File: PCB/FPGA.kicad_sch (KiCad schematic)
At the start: 7 parts

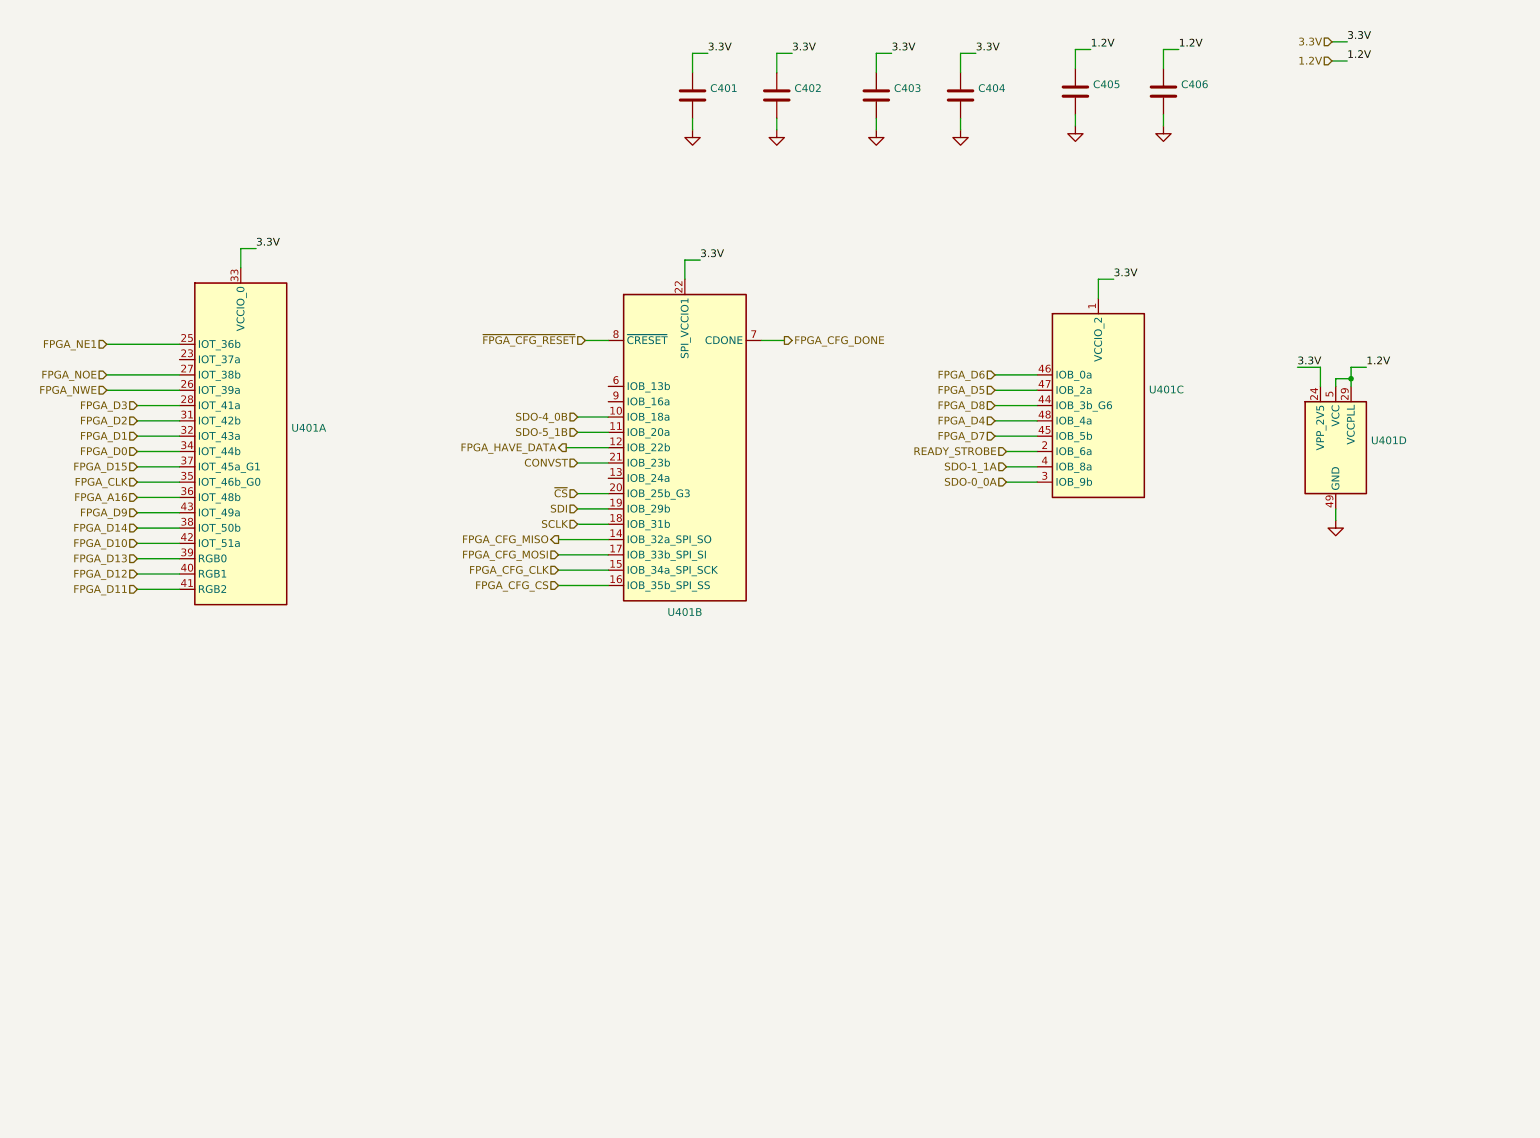
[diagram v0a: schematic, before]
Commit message: New version with FTDI chip instead of STM32 and ICE40HX FPGA instead of slower ones
Signed-off-by: Alexis Jeandet <alexis.jeandet@member.fsf.org>
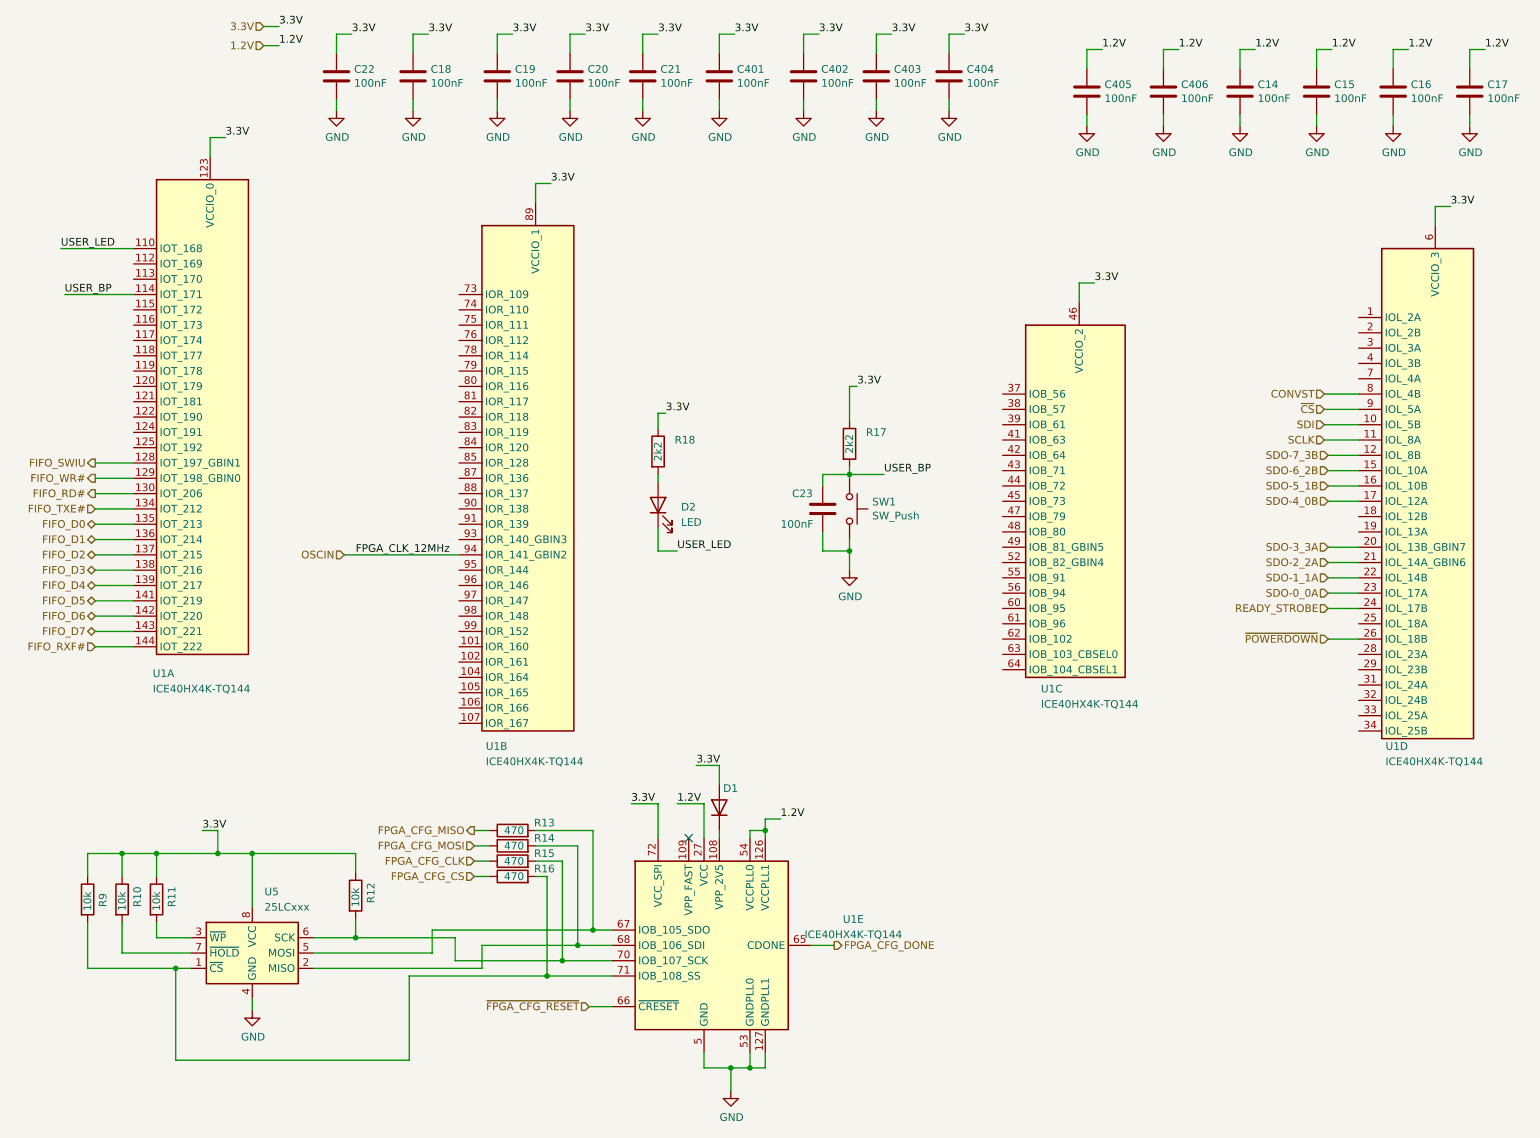
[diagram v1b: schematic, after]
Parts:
- removed U401: (no value), symbol FPGA_Lattice:ICE40UP5K-SG48ITR
- added C14, C15, C16, C17, C18, C19, C20, C21, C22, C23: 100nF, Capacitor_SMD:C_0402_1005Metric_Pad0.74x0.62mm_HandSolder, symbol Device:C
- added D1: 1N4148WT, Diode_SMD:D_SOD-523, symbol Diode:1N4148WT
- added D2: LED, Diode_SMD:D_0603_1608Metric_Pad1.05x0.95mm_HandSolder, symbol Device:LED
- added R10, R11, R12, R9: 10k, Resistor_SMD:R_0402_1005Metric_Pad0.72x0.64mm_HandSolder, symbol Device:R
- added R13, R14, R15, R16: 470, Resistor_SMD:R_0402_1005Metric_Pad0.72x0.64mm_HandSolder, symbol Device:R
- added R17, R18: 2k2, Resistor_SMD:R_0402_1005Metric_Pad0.72x0.64mm_HandSolder, symbol Device:R
- added SW1: SW_Push, Button_Switch_SMD:SW_SPST_TL3342, symbol Switch:SW_Push
- added U1: ICE40HX4K-TQ144, Package_QFP:TQFP-144_20x20mm_P0.5mm, symbol FPGA_Lattice:ICE40HX4K-TQ144
- added U5: 25LCxxx, Package_SO:SOP-8_3.9x4.9mm_P1.27mm, symbol Memory_EEPROM:25LCxxx
- C401, C402, C403, C404, C405, C406: value (none) -> 100nF; footprint (none) -> Capacitor_SMD:C_0402_1005Metric_Pad0.74x0.62mm_HandSolder
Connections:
- net 1.2V: now also C14.1, C15.1, C16.1, C17.1, U1.111 (VCC), U1.126 (VCCPLL1), U1.27 (VCC), U1.40 (VCC), U1.54 (VCCPLL0), U1.92 (VCC)
- net 3.3V: now also C18.1, C19.1, C20.1, C21.1, C22.1, D1.2 (A), R10.1, R11.1, R12.1, R17.1, R18.1, R9.1, U1.100 (VCCIO_1), U1.123 (VCCIO_0), U1.131 (VCCIO_0), U1.30 (VCCIO_3), U1.46 (VCCIO_2), U1.57 (VCCIO_2), U1.6 (VCCIO_3), U1.72 (VCC_SPI), U1.89 (VCCIO_1), U5.8 (VCC)
- net CONVST: now also U1.8 (IOL_4B)
- net FPGA_CFG_CLK: now also R15.1
- net FPGA_CFG_CS: now also R16.1
- net FPGA_CFG_DONE: now also U1.65 (CDONE)
- net FPGA_CFG_MISO: now also R13.1
- net FPGA_CFG_MOSI: now also R14.1
- net GND: now also C14.2, C15.2, C16.2, C17.2, C18.2, C19.2, C20.2, C21.2, C22.2, C23.2, SW1.2, U1.103 (GND), U1.127 (GNDPLL1), U1.13 (GND), U1.132 (GND), U1.14 (GND), U1.140 (GND), U1.5 (GND), U1.53 (GNDPLL0), U1.59 (GND), U1.69 (GND), U1.86 (GND), U5.4 (GND)
- net READY_STROBE: now also U1.24 (IOL_17B)
- net SCLK: now also U1.11 (IOL_8A)
- net SDI: now also U1.10 (IOL_5B)
- net SDO-0_0A: now also U1.23 (IOL_17A)
- net SDO-1_1A: now also U1.22 (IOL_14B)
- net SDO-4_0B: now also U1.17 (IOL_12A)
- net SDO-5_1B: now also U1.16 (IOL_10B)
- net ~{CS}: now also U1.9 (IOL_5A)
- net ~{FPGA_CFG_RESET}: now also U1.66 (~{CRESET})
- new net: D2.2 (A), R18.2
- new net: R11.2, U5.3 (~{WP})
- new net: D1.1 (K), U1.108 (VPP_2V5)
- new net: R13.2, U1.67 (IOB_105_SDO), U5.5 (MOSI)
- new net: R14.2, U1.68 (IOB_106_SDI), U5.2 (MISO)
- new net: R12.2, R15.2, U1.70 (IOB_107_SCK), U5.6 (SCK)
- new net: R16.2, R9.2, U1.71 (IOB_108_SS), U5.1 (~{CS})
- new net: R10.2, U5.7 (~{HOLD})
- new net FIFO_D0: U1.135 (IOT_213)
- new net FIFO_D1: U1.136 (IOT_214)
- new net FIFO_D2: U1.137 (IOT_215)
- new net FIFO_D3: U1.138 (IOT_216)
- new net FIFO_D4: U1.139 (IOT_217)
- new net FIFO_D5: U1.141 (IOT_219)
- new net FIFO_D6: U1.142 (IOT_220)
- new net FIFO_D7: U1.143 (IOT_221)
- new net FIFO_RD#: U1.130 (IOT_206)
- new net FIFO_RXF#: U1.144 (IOT_222)
- new net FIFO_SWIU: U1.128 (IOT_197_GBIN1)
- new net FIFO_TXE#: U1.134 (IOT_212)
- new net FIFO_WR#: U1.129 (IOT_198_GBIN0)
- new net OSCIN: U1.94 (IOR_141_GBIN2)
- new net SDO-2_2A: U1.21 (IOL_14A_GBIN6)
- new net SDO-3_3A: U1.20 (IOL_13B_GBIN7)
- new net SDO-6_2B: U1.15 (IOL_10A)
- new net SDO-7_3B: U1.12 (IOL_8B)
- new net USER_BP: C23.1, R17.2, SW1.1, U1.114 (IOT_171)
- new net USER_LED: D2.1 (K), U1.110 (IOT_168)
- new net ~{POWERDOWN}: U1.26 (IOL_18B)
- no-connect marks 0 -> 1
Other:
- moved on the sheet: C401, C402, C403, C404, C405

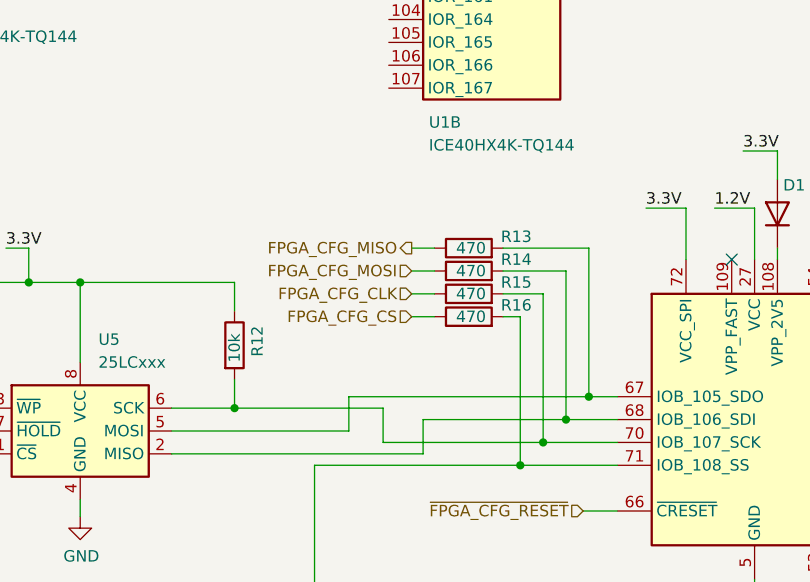
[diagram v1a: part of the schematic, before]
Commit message: adds UGA and few sch libs update
Signed-off-by: Alexis Jeandet <alexis.jeandet@member.fsf.org>
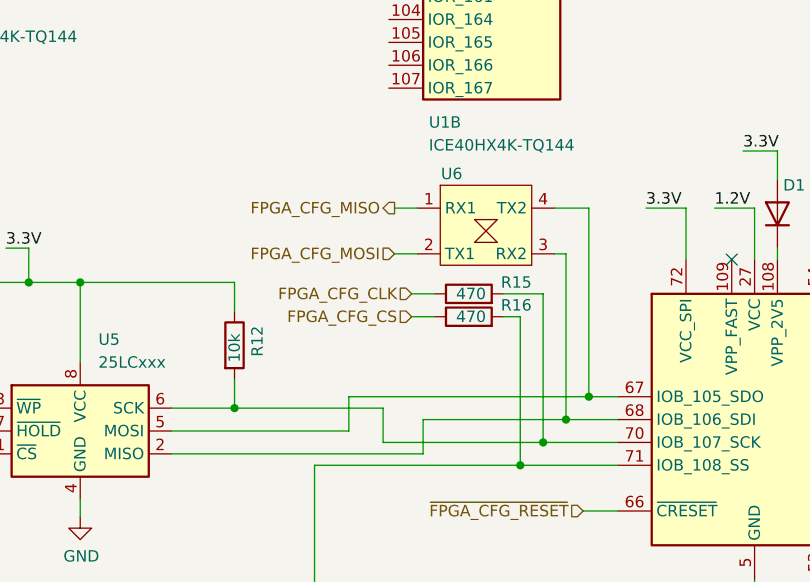
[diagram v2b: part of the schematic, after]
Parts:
- removed R13, R14: 470, Resistor_SMD:R_0402_1005Metric_Pad0.72x0.64mm_HandSolder, symbol Device:R
- added U6: UGA, UGA:UGA_0603, symbol UGA:UGA
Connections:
- net FPGA_CFG_MISO: now also U6.1 (RX1)
- net FPGA_CFG_MOSI: now also U6.2 (TX1)
- net at U1.67 (IOB_105_SDO), U5.5 (MOSI): now also U6.4 (TX2)
- net at U1.68 (IOB_106_SDI), U5.2 (MISO): now also U6.3 (RX2)
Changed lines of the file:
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@@
+    (stroke (width 0) (type default) (color 0 0 0 0))
+  )
+  (wire (pts (xy 114.935 149.225) (xy 113.665 149.225))
     (stroke (width 0) (type default) (color 0 0 0 0))
   )
@@
     (stroke (width 0) (type default) (color 0 0 0 0))
   )
+  (wire (pts (xy 114.935 149.225) (xy 114.935 167.64))
+    (stroke (width 0) (type default) (color 0 0 0 0))
+  )
   (wire (pts (xy 128.27 79.375) (xy 128.27 81.915))
     (stroke (width 0) (type default) (color 0 0 0 0))
@@
     (stroke (width 0) (type default) (color 0 0 0 0))
   )
-  (wire (pts (xy 107.95 148.59) (xy 117.475 148.59))
-    (stroke (width 0) (type default) (color 0 0 0 0))
-  )
-  (wire (pts (xy 97.79 151.13) (xy 100.33 151.13))
+  (wire (pts (xy 95.885 149.225) (xy 98.425 149.225))
     (stroke (width 0) (type default) (color 0 0 0 0))
   )
@@
     (stroke (width 0) (type default) (color 0 0 0 0))
   )
-  (wire (pts (xy 117.475 148.59) (xy 117.475 165.1))
-    (stroke (width 0) (type default) (color 0 0 0 0))
-  )
   (wire (pts (xy 90.805 165.1) (xy 117.475 165.1))
     (stroke (width 0) (type default) (color 0 0 0 0))
@@
     (stroke (width 0) (type default) (color 0 0 0 0))
   )
-  (wire (pts (xy 107.95 151.13) (xy 114.935 151.13))
-    (stroke (width 0) (type default) (color 0 0 0 0))
-  )
   (wire (pts (xy 60.96 152.4) (xy 78.105 152.4))
     (stroke (width 0) (type default) (color 0 0 0 0))
@@
     (stroke (width 0) (type default) (color 0 0 0 0))
   )
-  (wire (pts (xy 97.79 148.59) (xy 100.33 148.59))
+  (wire (pts (xy 95.885 144.145) (xy 98.425 144.145))
     (stroke (width 0) (type default) (color 0 0 0 0))
   )
@@
     (stroke (width 0) (type default) (color 0 0 0 0))
   )
+  (wire (pts (xy 113.665 144.145) (xy 117.475 144.145))
+    (stroke (width 0) (type default) (color 0 0 0 0))
+  )
   (wire (pts (xy 29.21 52.07) (xy 41.275 52.07))
     (stroke (width 0) (type default) (color 0 0 0 0))
@@
     (stroke (width 0) (type default) (color 0 0 0 0))
   )
-  (wire (pts (xy 114.935 151.13) (xy 114.935 167.64))
-    (stroke (width 0) (type default) (color 0 0 0 0))
-  )
   (wire (pts (xy 152.4 29.21) (xy 152.4 27.305))
     (stroke (width 0) (type default) (color 0 0 0 0))
@@
   )
   (wire (pts (xy 107.95 153.67) (xy 112.395 153.67))
+    (stroke (width 0) (type default) (color 0 0 0 0))
+  )
+  (wire (pts (xy 117.475 144.145) (xy 117.475 165.1))
     (stroke (width 0) (type default) (color 0 0 0 0))
   )
@@
     (effects (font (size 1.27 1.27)) (justify right))
   )
-  (hierarchical_label "FPGA_CFG_MOSI" (shape input) (at 97.79 151.13 180)
+  (hierarchical_label "FPGA_CFG_MOSI" (shape input) (at 95.885 149.225 180)
     (effects (font (size 1.27 1.27)) (justify right))
   )
@@
     (effects (font (size 1.27 1.27)) (justify right))
   )
-  (hierarchical_label "FPGA_CFG_MISO" (shape output) (at 97.79 148.59 180)
+  (hierarchical_label "FPGA_CFG_MISO" (shape output) (at 95.885 144.145 180)
     (effects (font (size 1.27 1.27)) (justify right))
   )
@@
     (pin "92")
   )
-  (symbol (lib_id "Device:R") (at 104.14 151.13 90) (unit 1)
-    (in_bom yes) (on_board yes)
-    (property "Reference" "R14" (id 0) (at 111.125 149.86 90)
-      (effects (font (size 1.27 1.27)) (justify left))
-    )
-    (property "Value" "470" (id 1) (at 106.045 151.13 90)
-      (effects (font (size 1.27 1.27)) (justify left))
-    )
-    (property "Footprint" "Resistor_SMD:R_0402_1005Metric_Pad0.72x0.64mm_HandSolder" (id 2) (at 104.14 152.908 90)
-      (effects (font (size 1.27 1.27)) hide)
-    )
-    (property "Datasheet" "~" (id 3) (at 104.14 151.13 0)
-      (effects (font (size 1.27 1.27)) hide)
-    )
-    (pin "1")
-    (pin "2")
-  )
   (symbol (lib_id "Device:R") (at 39.37 160.02 0) (unit 1)
     (in_bom yes) (on_board yes)
@@
     (pin "1")
   )
+  (symbol (lib_id "UGA:UGA") (at 100.965 150.495 0) (unit 1)
+    (in_bom no) (on_board yes)
+    (property "Reference" "U6" (id 0) (at 102.235 140.335 0))
+    (property "Value" "UGA" (id 1) (at 106.045 138.43 0)
+      (effects (font (size 1.27 1.27)) hide)
+    )
+    (property "Footprint" "UGA:UGA_0603" (id 2) (at 100.965 150.495 0)
+      (effects (font (size 1.27 1.27)) hide)
+    )
+    (property "Datasheet" "" (id 3) (at 100.965 150.495 0)
+      (effects (font (size 1.27 1.27)) hide)
+    )
+    (pin "1")
+    (pin "2")
+    (pin "3")
+    (pin "4")
+  )
   (symbol (lib_id "power:GND") (at 125.73 29.21 0) (unit 1)
     (in_bom yes) (on_board yes)
@@
       (effects (font (size 1.27 1.27)) hide)
     )
-    (pin "1")
-    (pin "2")
-  )
-  (symbol (lib_id "Device:R") (at 104.14 148.59 90) (unit 1)
-    (in_bom yes) (on_board yes)
-    (property "Reference" "R13" (id 0) (at 111.125 147.32 90)
-      (effects (font (size 1.27 1.27)) (justify left))
-    )
-    (property "Value" "470" (id 1) (at 106.045 148.59 90)
-      (effects (font (size 1.27 1.27)) (justify left))
-    )
-    (property "Footprint" "Resistor_SMD:R_0402_1005Metric_Pad0.72x0.64mm_HandSolder" (id 2) (at 104.14 150.368 90)
-      (effects (font (size 1.27 1.27)) hide)
-    )
-    (property "Datasheet" "~" (id 3) (at 104.14 148.59 0)
-      (effects (font (size 1.27 1.27)) hide)
-    )
